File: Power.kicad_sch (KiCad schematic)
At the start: 48 parts, among them SW901 DP3T, U901 BQ24075, U902 TPS7A0533PDBV, U903 LP5907MFX-3.3

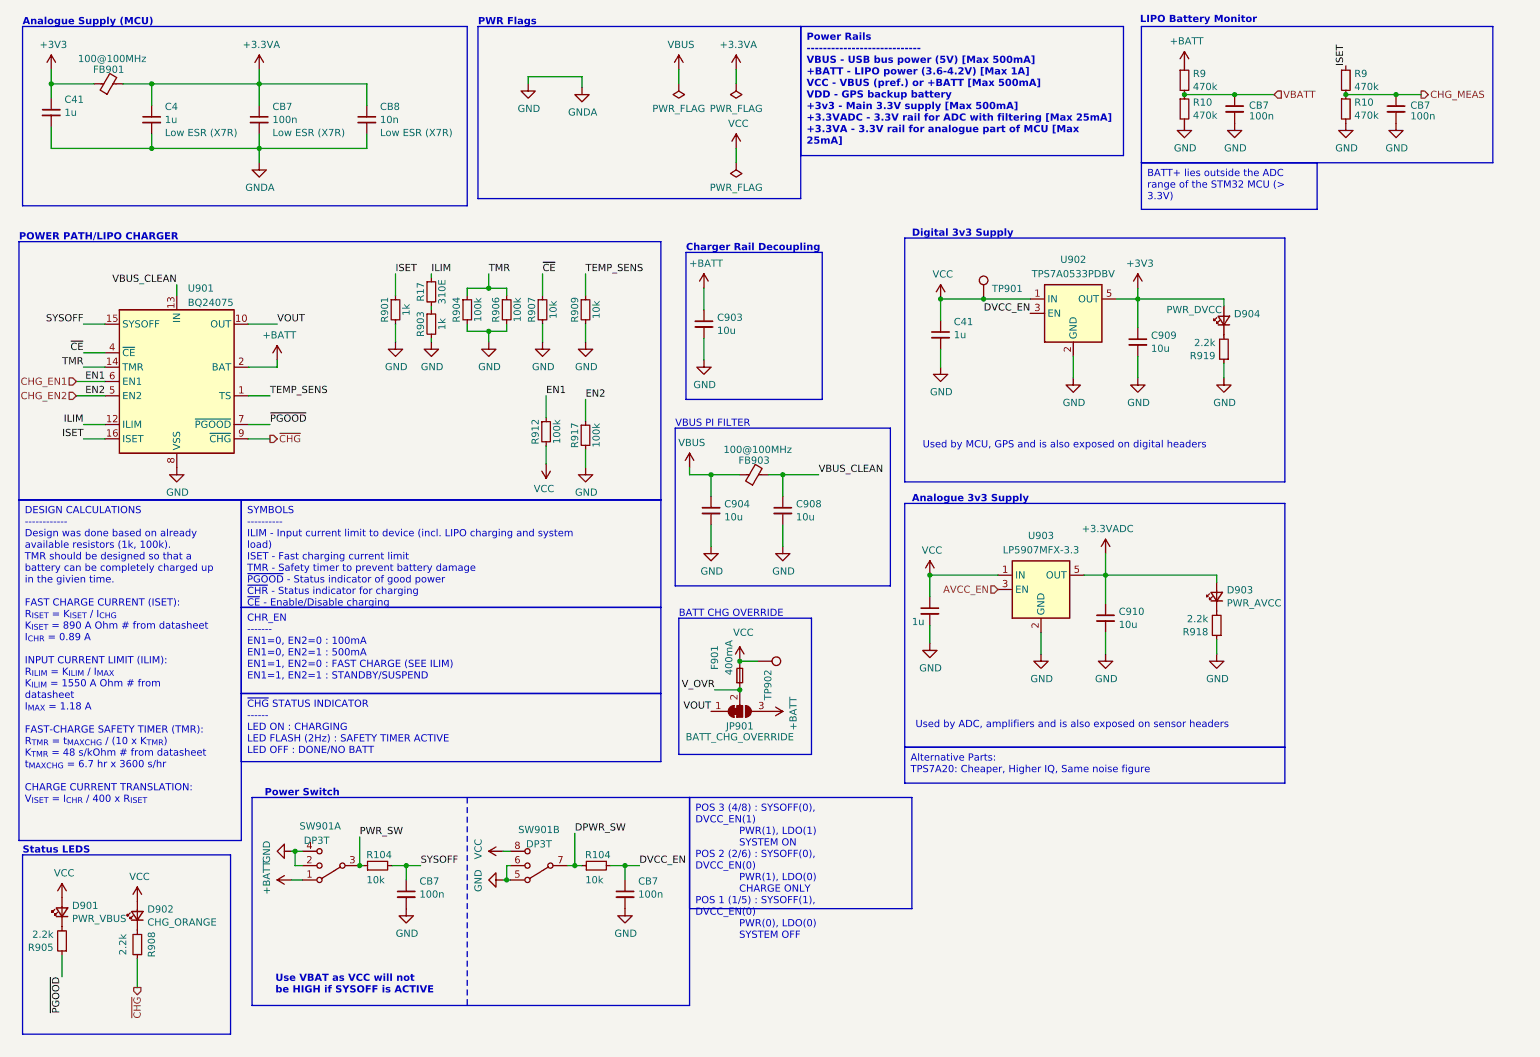
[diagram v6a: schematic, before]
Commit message: (sch) change to 100k pull-ups
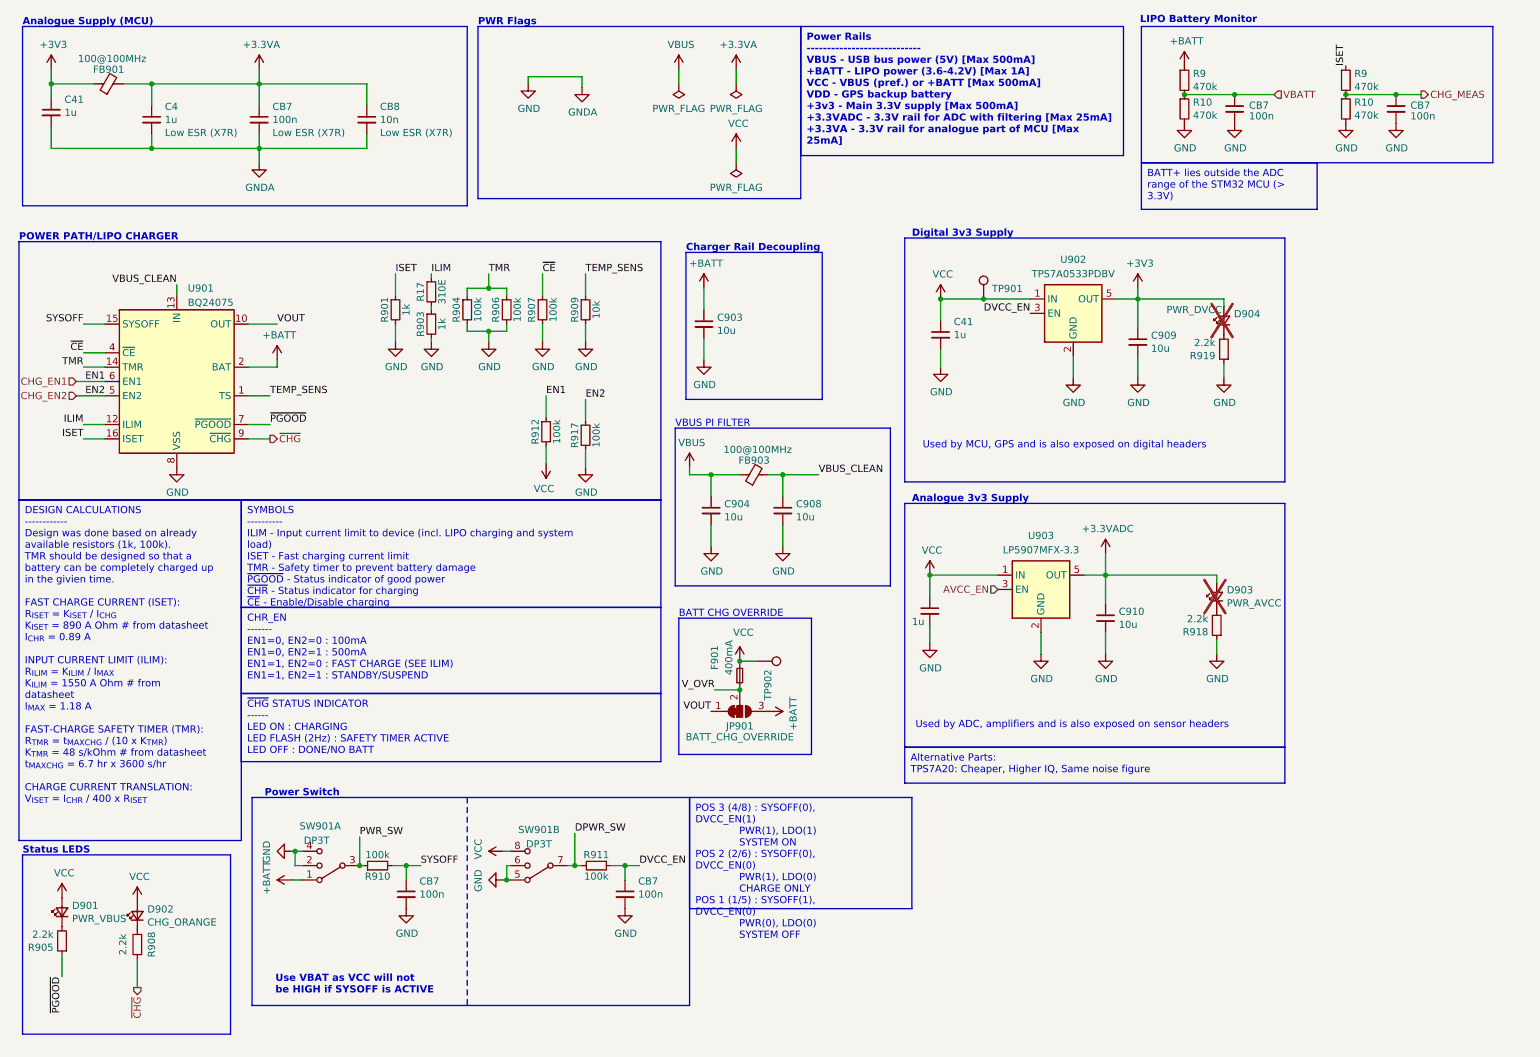
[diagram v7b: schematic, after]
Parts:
- removed R104 (x2): 10k, Resistor_SMD:R_0402_1005Metric, symbol Device:R_Small
- added R910, R911: 100k, Resistor_SMD:R_0402_1005Metric, symbol Device:R_Small
- D903: now not fitted
- D904: now not fitted; now left out of the parts list
- R907: value 10k -> 100k; MPN RT0402FRE1310KL -> RT0402FRE07100KL
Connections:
- net DPWR_SW: now also R911.2
- net DVCC_EN: now also R911.1
- net PWR_SW: now also R910.1
- net SYSOFF: now also R910.2
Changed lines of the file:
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@@
-    )
-  )
-  (symbol (lib_id "Device:R_Small") (at 107.315 66.675 0) (unit 1)
-    (in_bom yes) (on_board yes) (dnp no)
-    (property "Reference" "R907" (at 105.41 66.675 90)
-      (effects (font (size 1.27 1.27)))
-    )
-    (property "Value" "10k" (at 109.22 66.675 90)
-      (effects (font (size 1.27 1.27)))
-    )
-    (property "Footprint" "Resistor_SMD:R_0402_1005Metric" (at 107.315 66.675 0)
-      (effects (font (size 1.27 1.27)) hide)
-    )
-    (property "Datasheet" "~" (at 107.315 66.675 0)
-      (effects (font (size 1.27 1.27)) hide)
-    )
-    (property "MPN" "RT0402FRE1310KL" (at 107.315 66.675 0)
-      (effects (font (size 1.27 1.27)) hide)
-    )
-    (property "Mfr." "Yageo" (at 107.315 66.675 0)
-      (effects (font (size 1.27 1.27)) hide)
-    )
-    (pin "1")
-    (pin "2")
-    (instances
-      (project "kleinvoet"
-        (path "/4185c36c-c66e-4dbd-be5d-841e551f4885/00000000-0000-0000-0000-00005eede770"
-          (reference "R907") (unit 1)
-        )
-      )
     )
   )
@@
     )
   )
+  (symbol (lib_id "Device:R_Small") (at 107.315 66.675 0) (unit 1)
+    (in_bom yes) (on_board yes) (dnp no)
+    (property "Reference" "R907" (at 105.41 66.675 90)
+      (effects (font (size 1.27 1.27)))
+    )
+    (property "Value" "100k" (at 109.22 66.675 90)
+      (effects (font (size 1.27 1.27)))
+    )
+    (property "Footprint" "Resistor_SMD:R_0402_1005Metric" (at 107.315 66.675 0)
+      (effects (font (size 1.27 1.27)) hide)
+    )
+    (property "Datasheet" "~" (at 107.315 66.675 0)
+      (effects (font (size 1.27 1.27)) hide)
+    )
+    (property "MPN" "RT0402FRE07100KL" (at 107.315 66.675 0)
+      (effects (font (size 1.27 1.27)) hide)
+    )
+    (property "Mfr." "Yageo" (at 107.315 66.675 0)
+      (effects (font (size 1.27 1.27)) hide)
+    )
+    (pin "1")
+    (pin "2")
+    (instances
+      (project "kleinvoet"
+        (path "/4185c36c-c66e-4dbd-be5d-841e551f4885/00000000-0000-0000-0000-00005eede770"
+          (reference "R907") (unit 1)
+        )
+      )
+    )
+  )
   (symbol (lib_id "Device:R_Small") (at 220.98 31.115 0) (unit 1)
     (in_bom yes) (on_board yes) (dnp no)
@@
   )
   (symbol (lib_id "Device:LED_Small") (at 226.695 117.475 90) (unit 1)
-    (in_bom yes) (on_board yes) (dnp no)
+    (in_bom yes) (on_board yes) (dnp yes)
     (property "Reference" "D903" (at 228.473 116.3066 90)
       (effects (font (size 1.27 1.27)) (justify right))
@@
     )
     (property "Mfr." "ROHM Semiconductor" (at 226.695 117.475 90)
+      (effects (font (size 1.27 1.27)) hide)
+    )
+    (property "Sim.Enable" "0" (at 226.695 117.475 0)
       (effects (font (size 1.27 1.27)) hide)
     )
@@
         (path "/4185c36c-c66e-4dbd-be5d-841e551f4885/00000000-0000-0000-0000-00005eede770"
           (reference "TP901") (unit 1)
+        )
+      )
+    )
+  )
+  (symbol (lib_id "Device:R_Small") (at 78.105 165.1 90) (unit 1)
+    (in_bom yes) (on_board yes) (dnp no)
+    (property "Reference" "R910" (at 78.105 167.005 90)
+      (effects (font (size 1.27 1.27)))
+    )
+    (property "Value" "100k" (at 78.105 163.195 90)
+      (effects (font (size 1.27 1.27)))
+    )
+    (property "Footprint" "Resistor_SMD:R_0402_1005Metric" (at 78.105 165.1 0)
+      (effects (font (size 1.27 1.27)) hide)
+    )
+    (property "Datasheet" "~" (at 78.105 165.1 0)
+      (effects (font (size 1.27 1.27)) hide)
+    )
+    (property "MPN" "RT0402FRE07100KL" (at 78.105 165.1 0)
+      (effects (font (size 1.27 1.27)) hide)
+    )
+    (property "Mfr." "Yageo" (at 78.105 165.1 0)
+      (effects (font (size 1.27 1.27)) hide)
+    )
+    (pin "1")
+    (pin "2")
+    (instances
+      (project "kleinvoet"
+        (path "/4185c36c-c66e-4dbd-be5d-841e551f4885/00000000-0000-0000-0000-00005eede770"
+          (reference "R910") (unit 1)
         )
       )
@@
         (path "/4185c36c-c66e-4dbd-be5d-841e551f4885/00000000-0000-0000-0000-00005eede770"
           (reference "#PWR0915") (unit 1)
-        )
-      )
-    )
-  )
-  (symbol (lib_id "Device:R_Small") (at 116.84 165.1 90) (unit 1)
-    (in_bom yes) (on_board yes) (dnp no)
-    (property "Reference" "R104" (at 119.38 163.195 90)
-      (effects (font (size 1.27 1.27)) (justify left))
-    )
-    (property "Value" "10k" (at 118.11 167.64 90)
-      (effects (font (size 1.27 1.27)) (justify left))
-    )
-    (property "Footprint" "Resistor_SMD:R_0402_1005Metric" (at 116.84 165.1 0)
-      (effects (font (size 1.27 1.27)) hide)
-    )
-    (property "Datasheet" "~" (at 116.84 165.1 0)
-      (effects (font (size 1.27 1.27)) hide)
-    )
-    (property "MPN" "RT0402FRE1310KL" (at 116.84 165.1 0)
-      (effects (font (size 1.27 1.27)) hide)
-    )
-    (property "Mfr." "Yageo" (at 116.84 165.1 0)
-      (effects (font (size 1.27 1.27)) hide)
-    )
-    (pin "1")
-    (pin "2")
-    (instances
-      (project "kleinvoet"
-        (path "/4185c36c-c66e-4dbd-be5d-841e551f4885"
-          (reference "R104") (unit 1)
-        )
-        (path "/4185c36c-c66e-4dbd-be5d-841e551f4885/00000000-0000-0000-0000-00005eede770"
-          (reference "R911") (unit 1)
         )
       )
@@
   )
   (symbol (lib_id "Device:LED_Small") (at 227.965 68.58 90) (unit 1)
-    (in_bom yes) (on_board yes) (dnp no)
+    (in_bom no) (on_board yes) (dnp yes)
     (property "Reference" "D904" (at 229.743 67.4116 90)
       (effects (font (size 1.27 1.27)) (justify right))
@@
     )
   )
+  (symbol (lib_id "Device:R_Small") (at 116.84 165.1 270) (unit 1)
+    (in_bom yes) (on_board yes) (dnp no)
+    (property "Reference" "R911" (at 116.84 163.195 90)
+      (effects (font (size 1.27 1.27)))
+    )
+    (property "Value" "100k" (at 116.84 167.005 90)
+      (effects (font (size 1.27 1.27)))
+    )
+    (property "Footprint" "Resistor_SMD:R_0402_1005Metric" (at 116.84 165.1 0)
+      (effects (font (size 1.27 1.27)) hide)
+    )
+    (property "Datasheet" "~" (at 116.84 165.1 0)
+      (effects (font (size 1.27 1.27)) hide)
+    )
+    (property "MPN" "RT0402FRE07100KL" (at 116.84 165.1 0)
+      (effects (font (size 1.27 1.27)) hide)
+    )
+    (property "Mfr." "Yageo" (at 116.84 165.1 0)
+      (effects (font (size 1.27 1.27)) hide)
+    )
+    (pin "1")
+    (pin "2")
+    (instances
+      (project "kleinvoet"
+        (path "/4185c36c-c66e-4dbd-be5d-841e551f4885/00000000-0000-0000-0000-00005eede770"
+          (reference "R911") (unit 1)
+        )
+      )
+    )
+  )
   (symbol (lib_id "power:GND") (at 226.695 127.635 0) (unit 1)
     (in_bom yes) (on_board yes) (dnp no)
@@
         )
       )
-    )
-  )
-  (symbol (lib_id "Device:R_Small") (at 78.105 165.1 90) (unit 1)
-    (in_bom yes) (on_board yes) (dnp no)
-    (property "Reference" "R104" (at 80.645 163.195 90)
-      (effects (font (size 1.27 1.27)) (justify left))
-    )
-    (property "Value" "10k" (at 79.375 167.64 90)
-      (effects (font (size 1.27 1.27)) (justify left))
-    )
-    (property "Footprint" "Resistor_SMD:R_0402_1005Metric" (at 78.105 165.1 0)
-      (effects (font (size 1.27 1.27)) hide)
-    )
-    (property "Datasheet" "~" (at 78.105 165.1 0)
-      (effects (font (size 1.27 1.27)) hide)
-    )
-    (property "MPN" "RT0402FRE1310KL" (at 78.105 165.1 0)
-      (effects (font (size 1.27 1.27)) hide)
-    )
-    (property "Mfr." "Yageo" (at 78.105 165.1 0)
-      (effects (font (size 1.27 1.27)) hide)
-    )
-    (pin "1")
-    (pin "2")
-    (instances
-      (project "kleinvoet"
-        (path "/4185c36c-c66e-4dbd-be5d-841e551f4885"
-          (reference "R104") (unit 1)
-        )
-        (path "/4185c36c-c66e-4dbd-be5d-841e551f4885/00000000-0000-0000-0000-00005eede770"
-          (reference "R910") (unit 1)
-        )
-      )

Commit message: (sch) update annotations
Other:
- note added: "DEFAULT: Fast Charge EN1=1, EN2=0"
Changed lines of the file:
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@@
     (effects (font (size 1.27 1.27)) (justify left top))
   )
-  (text_box "DESIGN CALCULATIONS\n------------\nDesign was done based on already available resistors (1k, 100k).\nTMR should be designed so that a battery can be completely charged up in the givien time.\n\nFAST CHARGE CURRENT (ISET):\nR_{ISET} = K_{ISET} / I_{CHG}\nK_{ISET} = 890 A Ohm # from datasheet\nI_{CHR} = 0.89 A\n\nINPUT CURRENT LIMIT (ILIM):\nR_{ILIM} = K_{ILIM} / I_{MAX}\nK_{ILIM} = 1550 A Ohm # from datasheet\nI_{MAX} = 1.18 A\n\nFAST-CHARGE SAFETY TIMER (TMR):\nR_{TMR} = t_{MAXCHG} / (10 x K_{TMR})\nK_{TMR} = 48 s/kOhm # from datasheet\nt_{MAXCHG} = 6.7 hr x 3600 s/hr\n\nCHARGE CURRENT TRANSLATION:\nV_{ISET} = I_{CHR} / 400 x R_{ISET}"
+  (text_box "DESIGN CALCULATIONS\n------------\nDesign was done based on already available resistors (1k, 100k).\nTMR should be designed so that a battery can be completely charged up in the givien time.\n\nFAST CHARGE CURRENT (ISET):\nR_{ISET} = K_{ISET} / I_{CHG}\nK_{ISET} = 890 A Ohm # from datasheet\nI_{CHR} = 0.89 A\n\nINPUT CURRENT LIMIT (ILIM):\nR_{ILIM} = K_{ILIM} / I_{MAX}\nK_{ILIM} = 1550 A Ohm # from datasheet\nI_{MAX} = 1.18 A\n\nFAST-CHARGE SAFETY TIMER (TMR):\nR_{TMR} = t_{MAXCHG} / (10 x K_{TMR})\nK_{TMR} = 48 s/kOhm # from datasheet\nt_{MAXCHG} = 6.7 hr x 3600 s/hr\n\nCHARGE CURRENT TRANSLATION:\nV_{ISET} = I_{CHR} / 200 x R_{ISET}"
     (at 14.605 100.33 0) (size 39.37 60.325)
     (stroke (width 0) (type default))
@@
     (effects (font (size 1.27 1.27)) (justify left top))
   )
-  (text_box "POS 3 (4/8) : SYSOFF(0), DVCC_EN(1)\n			  PWR(1), LDO(1)\n			  SYSTEM ON\nPOS 2 (2/6) : SYSOFF(0), DVCC_EN(0)\n			  PWR(1), LDO(0)\n			  CHARGE ONLY\nPOS 1 (1/5) : SYSOFF(1), DVCC_EN(0)\n			  PWR(0), LDO(0)\n			  SYSTEM OFF"
-    (at 133.35 153.035 0) (size 39.37 19.685)
+  (text_box "POS 3 (4/8) : SYSOFF(0), DVCC_EN(1)\n			 PWR(1), LDO(1)\n			 >> SYSTEM ON\n\nPOS 2 (2/6) : SYSOFF(0), DVCC_EN(0)\n			 PWR(1), LDO(0)\n			 >> CHARGE ONLY\n\nPOS 1 (1/5) : SYSOFF(1), DVCC_EN(0)\n			 PWR(0), LDO(0)\n			 >> SYSTEM OFF"
+    (at 133.35 153.035 0) (size 41.91 28.575)
     (stroke (width 0) (type default))
     (fill (type none))
@@
   )
   (text_box "BATT+ lies outside the ADC range of the STM32 MCU (> 3.3V)"
-    (at 213.36 40.64 0) (size 31.115 8.255)
+    (at 213.36 40.64 0) (size 41.91 8.255)
     (stroke (width 0) (type default))
     (fill (type none))
@@
     (effects (font (size 1.27 1.27) (thickness 0.254) bold) (justify left bottom))
   )
+  (text "DEFAULT: Fast Charge\nEN1=1, EN2=0" (at 105.41 99.06 0)
+    (effects (font (size 1.27 1.27)) (justify right bottom))
+  )
   (text "Analogue 3v3 Supply" (at 172.72 100.965 0)
